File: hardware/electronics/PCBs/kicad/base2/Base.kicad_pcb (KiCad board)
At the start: 2 copper layers, 79.4 x 68 mm, 103 parts, among them J1 HEADER2, J14 Conn_01x04, J3 USB_C_Receptacle_USB2.0_16P, SW1 D2LS-21, SW2 D2LS-21, U1 W25Q16JVSSIQ, U2 PMW3360DM-T2QU, U3 AP2202K-3.3, U4 AP2204K-1.8, U6 RP2350A, Y1 ABM8-272-T3

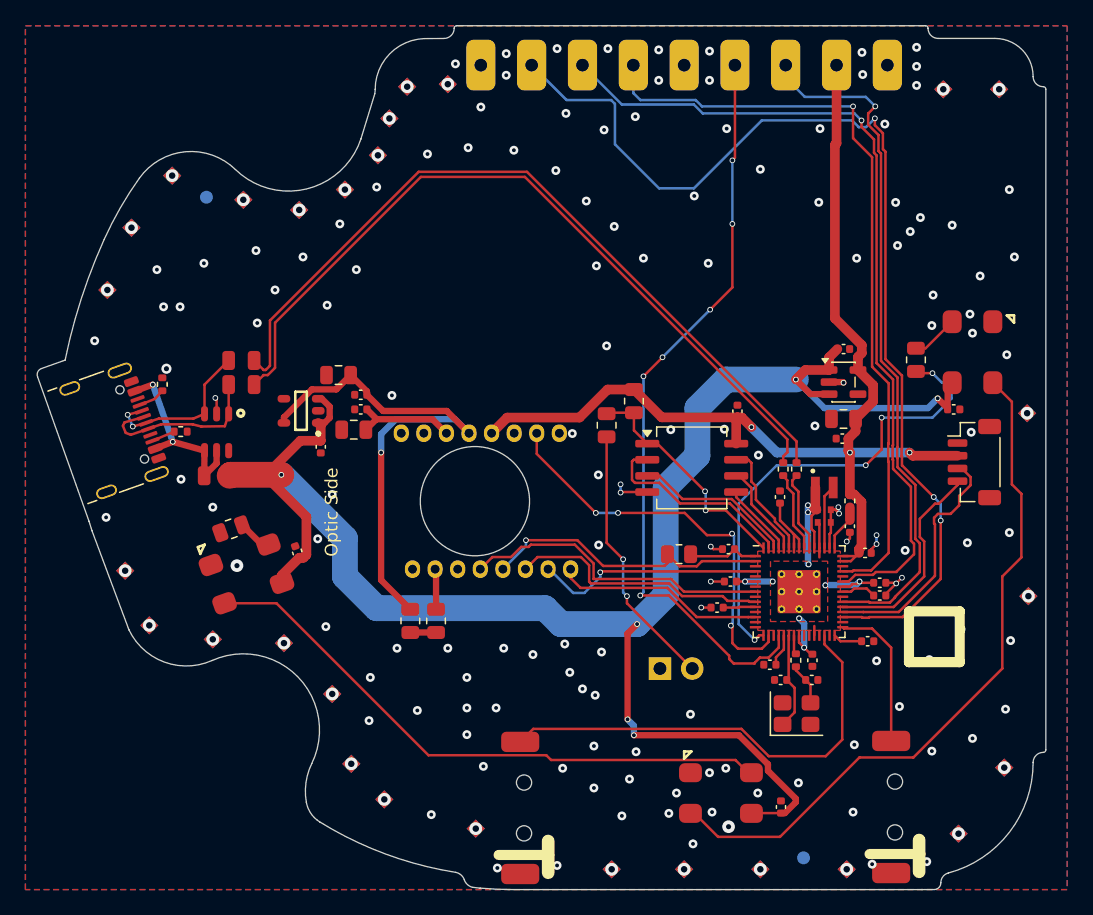
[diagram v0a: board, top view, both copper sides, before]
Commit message: Vertical neopixels
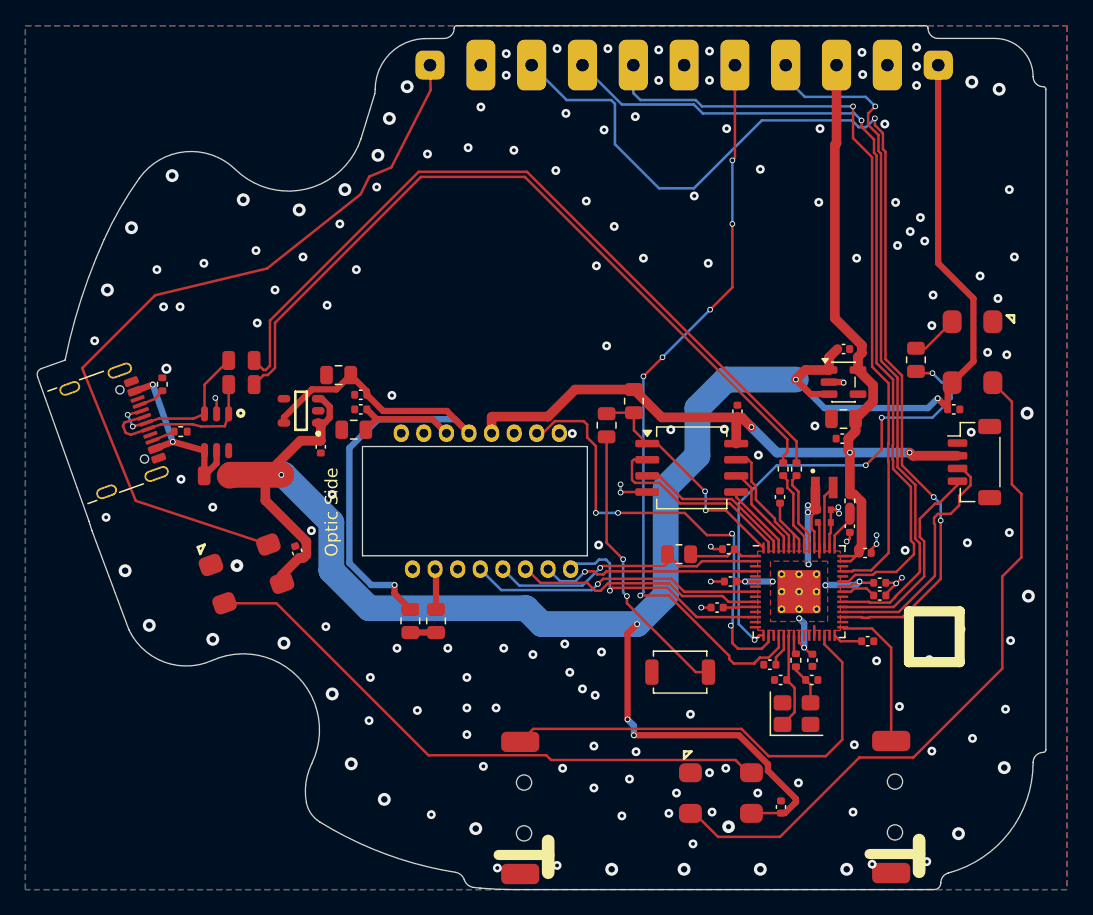
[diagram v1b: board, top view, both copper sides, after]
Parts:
- removed ? (x3): , 
- removed J1: HEADER2, Connectors:2x1
- removed MCH.FID.1, MCH.FID.2: IPC-7351 Fiducial 1mm, Mechanical:FIDUCIAL_1.5
- removed MCH.FID.3, MCH.FID.4: 1mm Fiducial for OpenPNP, Mechanical:FIDUCIAL-NEW
- removed MCH.SP.1, MCH.SP.10, MCH.SP.11, MCH.SP.12, MCH.SP.13, MCH.SP.14, MCH.SP.15, MCH.SP.16, MCH.SP.17, MCH.SP.18, MCH.SP.19, MCH.SP.2, MCH.SP.20, MCH.SP.21, MCH.SP.22, MCH.SP.23, MCH.SP.24, MCH.SP.25, MCH.SP.26, MCH.SP.27, MCH.SP.28, MCH.SP.3, MCH.SP.4, MCH.SP.5, MCH.SP.6, MCH.SP.7, MCH.SP.8, MCH.SP.9: Spark Gap, PCBFeatures:SparkGap
- removed R18: 1k, Resistor_SMD:R_0805_2012Metric
- added CJ10: PCBJointCastellationJoint, PCBFeatures:PCBJoint, F.Cu at (139.7, 74.1)
- added CJ11: PCBJointCastellationJoint, PCBFeatures:PCBJoint, F.Cu at (179.7, 74.1)
- added SW3: TS-1088-AR02016, Button_Switch_SMD:SW_SPST_TS-1088-xR020, F.Cu at (159.4, 121.9)
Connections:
- D5 pad 2: Net-(D5-DOUT) -> /LED/LEDDataOut
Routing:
- net /LED/V_USB: track 142.3 -> 169.6 mm
- net /MOS/1V8: track 41.0 -> 45.0 mm
- net /MCU/~{RESET}: track 32.3 -> 35.8 mm
- net Net-(D5-DOUT): track 2.71 -> 0.00 mm
- net /MCU/MOTION: track 16.5 -> 18.2 mm, vias 0 -> 1
- net /MCU/~{CS}: track 24.7 -> 23.1 mm, vias 0 -> 1
- net Net-(R1-Pad1): track 21.0 -> 22.4 mm
- net /MCU/MOSI: track 20.7 -> 19.7 mm
- net /MCU/MISO: track 23.3 -> 22.4 mm
- net /MCU/SCLK: track 18.0 -> 17.2 mm
- net +3.3V: track 111.4 -> 112.1 mm
- net GND: vias 171 -> 168
